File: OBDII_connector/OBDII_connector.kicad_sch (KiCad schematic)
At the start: 2 parts, among them J1 Conn_02x08_Counter_Clockwise, J2 Conn_01x02

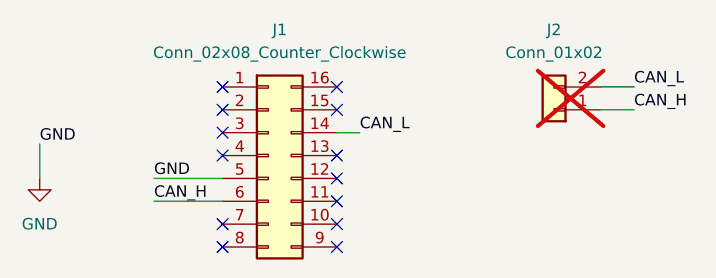
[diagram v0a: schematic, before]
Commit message: feat: add GND between OBDII connector & OBDII_RJ45
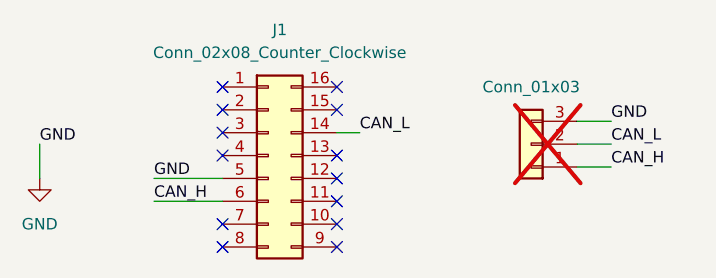
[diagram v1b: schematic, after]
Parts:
- removed J2: Conn_01x02, Connector_PinHeader_2.54mm:PinHeader_1x02_P2.54mm_Vertical, symbol Connector_Generic:Conn_01x02
- added J3: Conn_01x03, Connector_PinHeader_2.54mm:PinHeader_1x03_P2.54mm_Vertical, symbol Connector_Generic:Conn_01x03
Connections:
- net CAN_H: now also J3.1 (Pin_1)
- net CAN_L: now also J3.2 (Pin_2)
- net GND: now also J3.3 (Pin_3)
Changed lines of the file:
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@@
+	(wire
+		(pts
+			(xy 90.17 40.64) (xy 93.98 40.64)
+		)
+		(stroke
+			(width 0)
+			(type default)
+		)
+	)
+	(wire
+		(pts
+			(xy 90.17 38.1) (xy 93.98 38.1)
+		)
+		(stroke
+			(width 0)
+			(type default)
+		)
+	)
 	(wire
 		(pts
@@
 	(wire
 		(pts
-			(xy 92.71 31.75) (xy 96.52 31.75)
-		)
-		(stroke
-			(width 0)
-			(type default)
-		)
-	)
-	(wire
-		(pts
-			(xy 92.71 34.29) (xy 96.52 34.29)
+			(xy 90.17 35.56) (xy 93.98 35.56)
 		)
 		(stroke
@@
 	)
 	(label "CAN_L"
-		(at 96.52 31.75 0)
+		(at 93.98 38.1 0)
+		(effects
+			(font
+				(size 1.27 1.27)
+			)
+			(justify left bottom)
+		)
+	)
+	(label "GND"
+		(at 93.98 35.56 0)
 		(effects
 			(font
@@
 	)
 	(label "CAN_H"
-		(at 96.52 34.29 0)
+		(at 93.98 40.64 0)
 		(effects
 			(font
@@
 	)
 	(symbol
-		(lib_id "Connector_Generic:Conn_01x02")
-		(at 87.63 34.29 180)
-		(unit 1)
-		(exclude_from_sim no)
-		(in_bom yes)
-		(on_board yes)
-		(dnp yes)
-		(fields_autoplaced yes)
-		(property "Reference" "J2"
-			(at 87.63 25.4 0)
-			(effects
-				(font
-					(size 1.27 1.27)
-				)
-			)
-		)
-		(property "Value" "Conn_01x02"
-			(at 87.63 27.94 0)
-			(effects
-				(font
-					(size 1.27 1.27)
-				)
-			)
-		)
-		(property "Footprint" "Connector_PinHeader_2.54mm:PinHeader_1x02_P2.54mm_Vertical"
-			(at 87.63 34.29 0)
-			(effects
-				(font
-					(size 1.27 1.27)
-				)
-				(hide yes)
-			)
-		)
-		(property "Datasheet" "~"
-			(at 87.63 34.29 0)
-			(effects
-				(font
-					(size 1.27 1.27)
-				)
-				(hide yes)
-			)
-		)
-		(property "Description" "Generic connector, single row, 01x02, script generated (kicad-library-utils/schlib/autogen/connector/)"
-			(at 87.63 34.29 0)
-			(effects
-				(font
-					(size 1.27 1.27)
-				)
-				(hide yes)
-			)
-		)
-		(property "#MANUF" ""
-			(at 87.63 34.29 0)
-			(effects
-				(font
-					(size 1.27 1.27)
-				)
-				(hide yes)
-			)
-		)
-		(property "PROVEEDOR" ""
-			(at 87.63 34.29 0)
-			(effects
-				(font
-					(size 1.27 1.27)
-				)
-				(hide yes)
-			)
-		)
-		(pin "2"
-		)
-		(pin "1"
-		)
-		(instances
-			(project "OBDII_connector"
-				(path "/0a2cdc7f-9f05-4234-abf0-4d9ef4a14a4e"
-					(reference "J2")
-					(unit 1)
-				)
-			)
-		)
-	)
-	(symbol
 		(lib_id "Connector_Generic:Conn_02x08_Counter_Clockwise")
 		(at 55.88 39.37 0)
@@
 					(unit 1)
 				)
+			)
+		)
+	)
+	(symbol
+		(lib_id "Connector_Generic:Conn_01x03")
+		(at 85.09 38.1 180)
+		(unit 1)
+		(exclude_from_sim no)
+		(in_bom yes)
+		(on_board yes)
+		(dnp yes)
+		(fields_autoplaced yes)
+		(property "Reference" "J3"
+			(at 85.09 29.21 0)
+			(effects
+				(font
+					(size 1.27 1.27)
+				)
+				(hide yes)
+			)
+		)
+		(property "Value" "Conn_01x03"
+			(at 85.09 31.75 0)
+			(effects
+				(font
+					(size 1.27 1.27)
+				)
+			)
+		)
+		(property "Footprint" "Connector_PinHeader_2.54mm:PinHeader_1x03_P2.54mm_Vertical"
+			(at 85.09 38.1 0)
+			(effects
+				(font
+					(size 1.27 1.27)
+				)
+				(hide yes)
+			)
+		)
+		(property "Datasheet" "~"
+			(at 85.09 38.1 0)
+			(effects
+				(font
+					(size 1.27 1.27)
+				)
+				(hide yes)
+			)
+		)
+		(property "Description" "Generic connector, single row, 01x03, script generated (kicad-library-utils/schlib/autogen/connector/)"
+			(at 85.09 38.1 0)
+			(effects
+				(font
+					(size 1.27 1.27)
+				)
+				(hide yes)
+			)
+		)
+		(property "#MANUF" ""
+			(at 85.09 38.1 0)
+			(effects
+				(font
+					(size 1.27 1.27)
+				)
+				(hide yes)
+			)
+		)
+		(property "PROVEEDOR" ""
+			(at 85.09 38.1 0)
+			(effects
+				(font
+					(size 1.27 1.27)
+				)
+				(hide yes)
+			)
+		)
+		(pin "2"
+		)
+		(pin "1"
+		)
+		(pin "3"
+		)
+		(instances
+			(project "OBDII_connector"
+				(path "/0a2cdc7f-9f05-4234-abf0-4d9ef4a14a4e"
+					(reference "J3")
+					(unit 1)
+				)

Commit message: feat(hw): add lcsc parts
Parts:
- J3: #MANUF (none) -> PM254V-11-03-H85; LCSC# (none) -> C541850; now fitted
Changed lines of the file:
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@@
+			)
+		)
+		(property "LCSC#" ""
+			(at 55.88 39.37 0)
+			(effects
+				(font
+					(size 1.27 1.27)
+				)
 			)
 		)
@@
 		(in_bom yes)
 		(on_board yes)
-		(dnp yes)
+		(dnp no)
 		(fields_autoplaced yes)
 		(property "Reference" "J3"
@@
 			)
 		)
-		(property "Datasheet" "~"
+		(property "Datasheet" "https://www.lcsc.com/datasheet/lcsc_datasheet_2409302300_XFCN-PM254V-11-03-H85_C541850.pdf"
 			(at 85.09 38.1 0)
 			(effects
@@
 			)
 		)
-		(property "#MANUF" ""
+		(property "#MANUF" "PM254V-11-03-H85"
 			(at 85.09 38.1 0)
 			(effects
@@
 			)
 		)
+		(property "LCSC#" "C541850"
+			(at 85.09 38.1 0)
+			(effects
+				(font
+					(size 1.27 1.27)
+				)
+			)
+		)

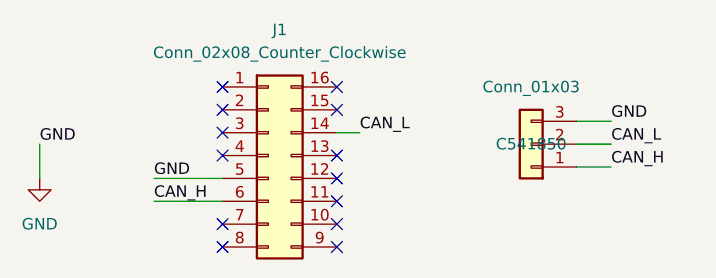
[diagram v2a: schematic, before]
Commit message: feat(Hw):Update_Labels
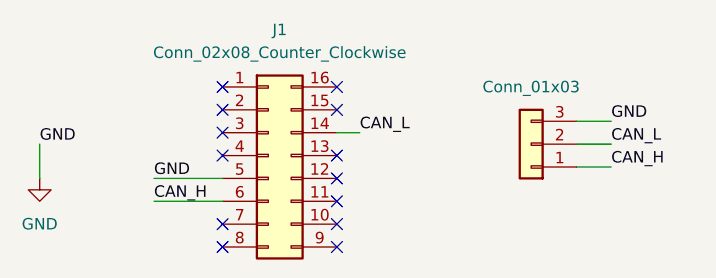
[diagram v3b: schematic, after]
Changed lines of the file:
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@@
 					(size 1.27 1.27)
 				)
+				(hide yes)
 			)
 		)
